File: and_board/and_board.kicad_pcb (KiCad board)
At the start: 2 copper layers, 39.7 x 31.6 mm, 12 parts, among them J1 SJ1-2503A, J2 SJ1-2503A, J3 SJ1-2503A, U1 SN74LS08N

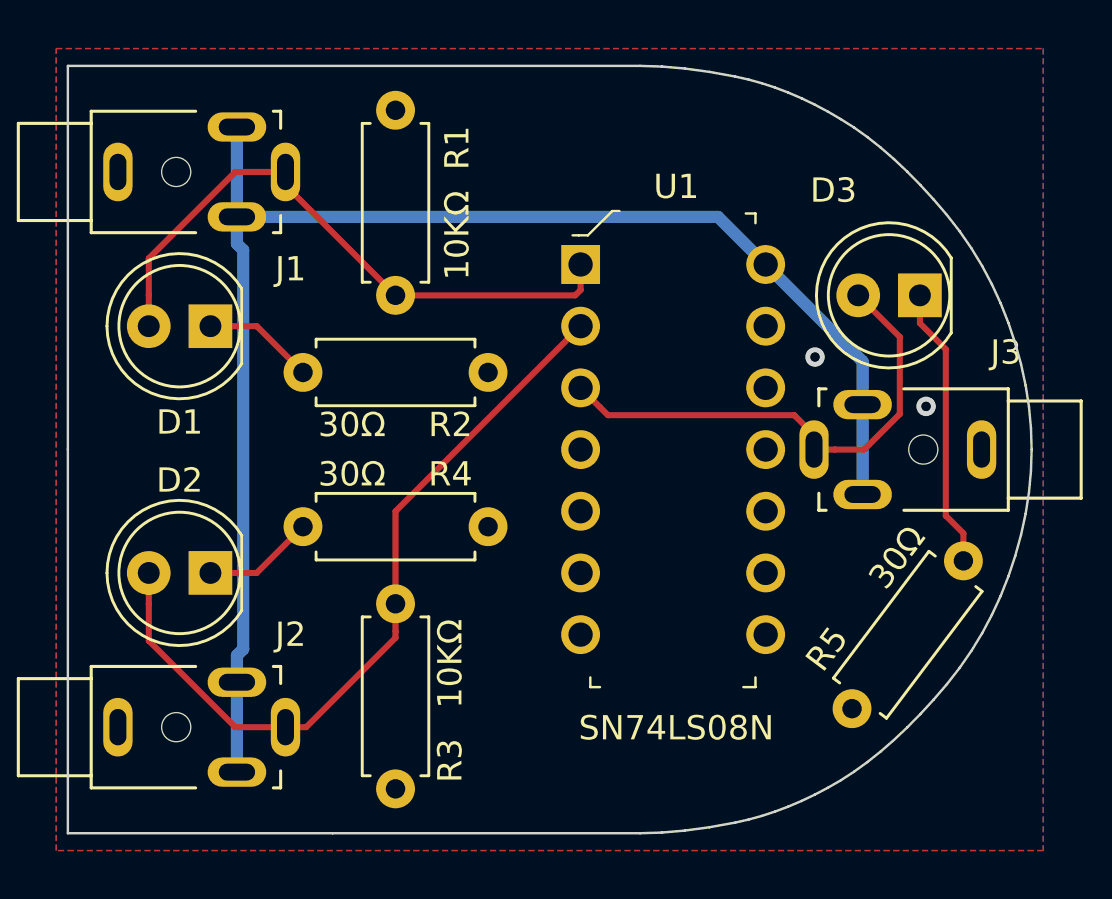
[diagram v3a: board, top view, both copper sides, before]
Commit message: Added truth table silk to and/or boards
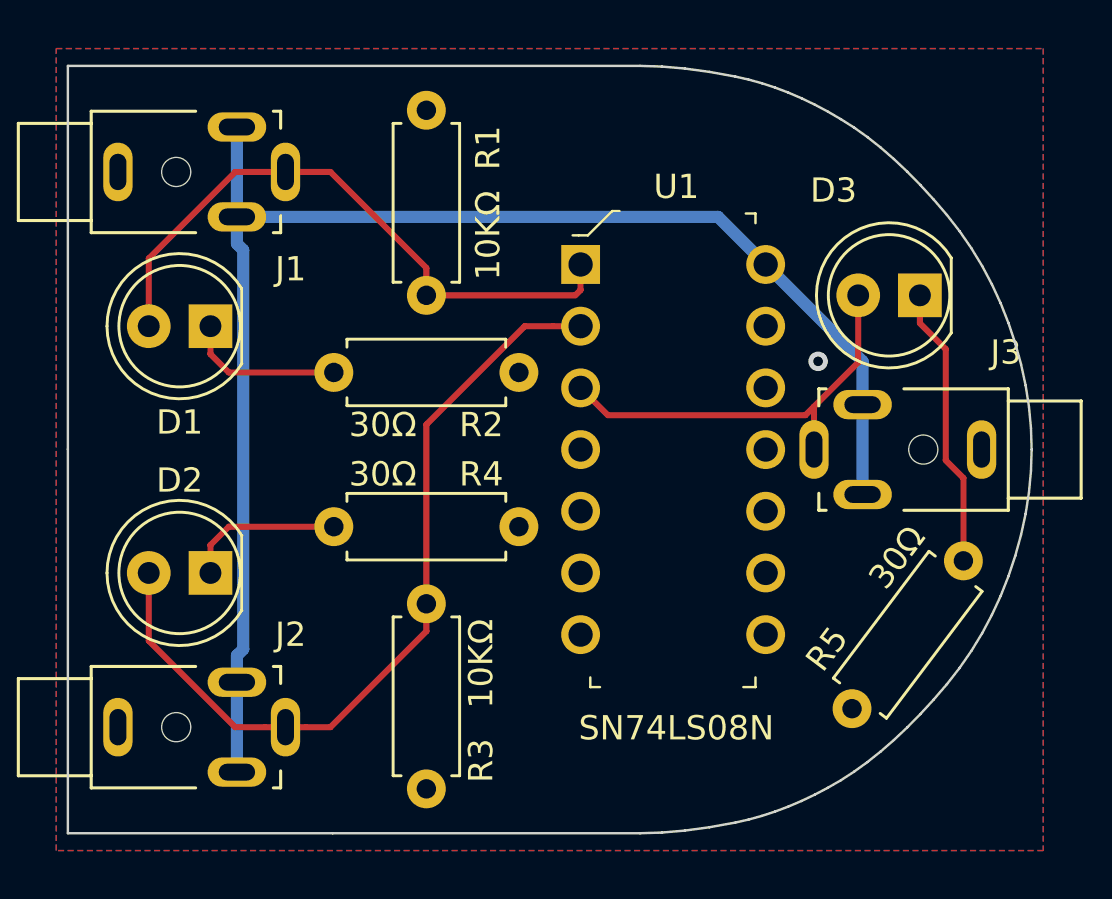
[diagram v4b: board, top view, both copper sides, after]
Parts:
- added Ref**: Val**, conduWIT_parts:and_truth_table, B.Cu at (149.4, 75.0)
- moved R1 1.27 mm to (144.8, 61.0)
- moved R2 1.27 mm to (148.6, 71.8)
- moved R3 1.27 mm to (144.8, 88.9)
- moved R4 1.27 mm to (148.6, 78.1)
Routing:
- net Net-(D3-Pad2): track 20.8 -> 17.3 mm
- net Net-(D2-Pad1): track 4.60 -> 6.54 mm
- net Net-(D1-Pad1): track 4.60 -> 6.54 mm
- net Net-(D2-Pad2): track 31.9 -> 33.9 mm
- net GND: vias 2 -> 1

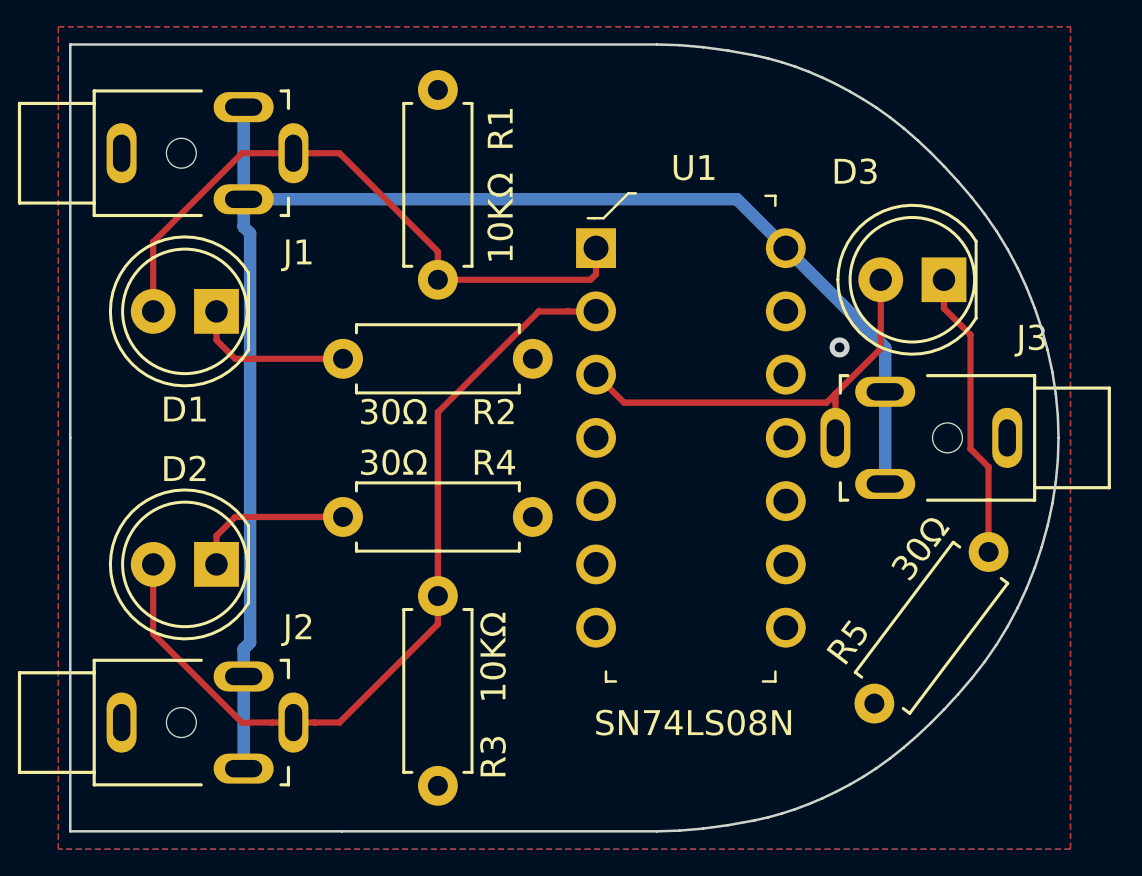
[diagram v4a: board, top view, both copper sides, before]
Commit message: Increased track width and clearance
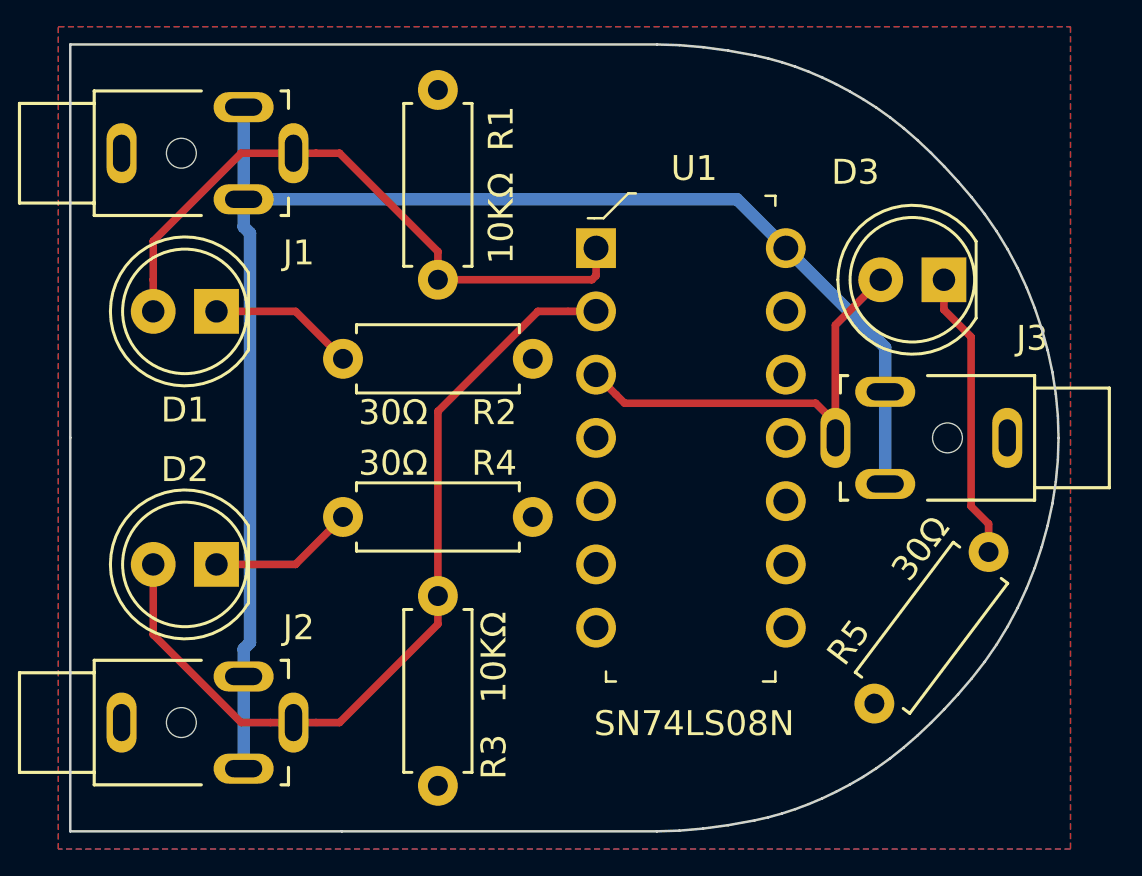
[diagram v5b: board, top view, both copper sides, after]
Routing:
- net Net-(D3-Pad2): track 17.3 -> 18.1 mm
- net Net-(D2-Pad1): track 6.54 -> 5.87 mm
- net Net-(D1-Pad1): track 6.54 -> 5.87 mm
- net GND: vias 1 -> 0
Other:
- net class Default: clearance 0.2 -> 0.19558; trace_width 0.25 -> 0.3048; via_dia 0.8 -> 0.5842; via_drill 0.4 -> 0.3302
- rule pad_to_mask_clearance: 0.051 -> 0
- rule trace_clearance: 0.2 -> 0.19558
- rule trace_min: 0.2 -> 0.3048
- rule via_min_drill: 0.3 -> 0.3302
- rule via_min_size: 0.4 -> 0.5842

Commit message: Final silkscreen touch-up
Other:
- board text added: "and_board 1.0.0 03/2020"
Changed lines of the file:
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@@
   (general
     (thickness 1.6)
-    (drawings 70)
+    (drawings 71)
     (tracks 51)
     (zones 0)
@@
     (0 F.Cu signal)
     (31 B.Cu signal)
-    (32 B.Adhes user hide)
-    (33 F.Adhes user hide)
-    (34 B.Paste user hide)
+    (32 B.Adhes user)
+    (33 F.Adhes user)
+    (34 B.Paste user)
     (35 F.Paste user)
-    (36 B.SilkS user hide)
+    (36 B.SilkS user)
     (37 F.SilkS user)
-    (38 B.Mask user hide)
+    (38 B.Mask user)
     (39 F.Mask user)
-    (40 Dwgs.User user hide)
-    (41 Cmts.User user hide)
-    (42 Eco1.User user hide)
-    (43 Eco2.User user hide)
+    (40 Dwgs.User user)
+    (41 Cmts.User user)
+    (42 Eco1.User user)
+    (43 Eco2.User user)
     (44 Edge.Cuts user)
-    (45 Margin user hide)
-    (46 B.CrtYd user hide)
-    (47 F.CrtYd user hide)
-    (48 B.Fab user hide)
-    (49 F.Fab user hide)
+    (45 Margin user)
+    (46 B.CrtYd user)
+    (47 F.CrtYd user)
+    (48 B.Fab user)
+    (49 F.Fab user)
   )
   (setup
@@
     (visible_elements 7FFFFFFF)
     (pcbplotparams
-      (layerselection 0x010fc_ffffffff)
-      (usegerberextensions false)
+      (layerselection 0x010f0_ffffffff)
+      (usegerberextensions true)
       (usegerberattributes false)
       (usegerberadvancedattributes false)
@@
       (outputformat 1)
       (mirror false)
-      (drillshape 1)
+      (drillshape 0)
       (scaleselection 1)
-      (outputdirectory ""))
+      (outputdirectory "mfg"))
   )
   (net 0 "")
@@
     )
   )
+  (gr_text "and_board\n1.0.0\n03/2020" (at 133.985 74.93 90) (layer B.SilkS)
+    (effects (font (size 1 1) (thickness 0.15)) (justify mirror))
+  )
   (gr_line (start 130.019472 59.132977) (end 153.574584 59.132977) (layer Edge.Cuts) (width 0.1))

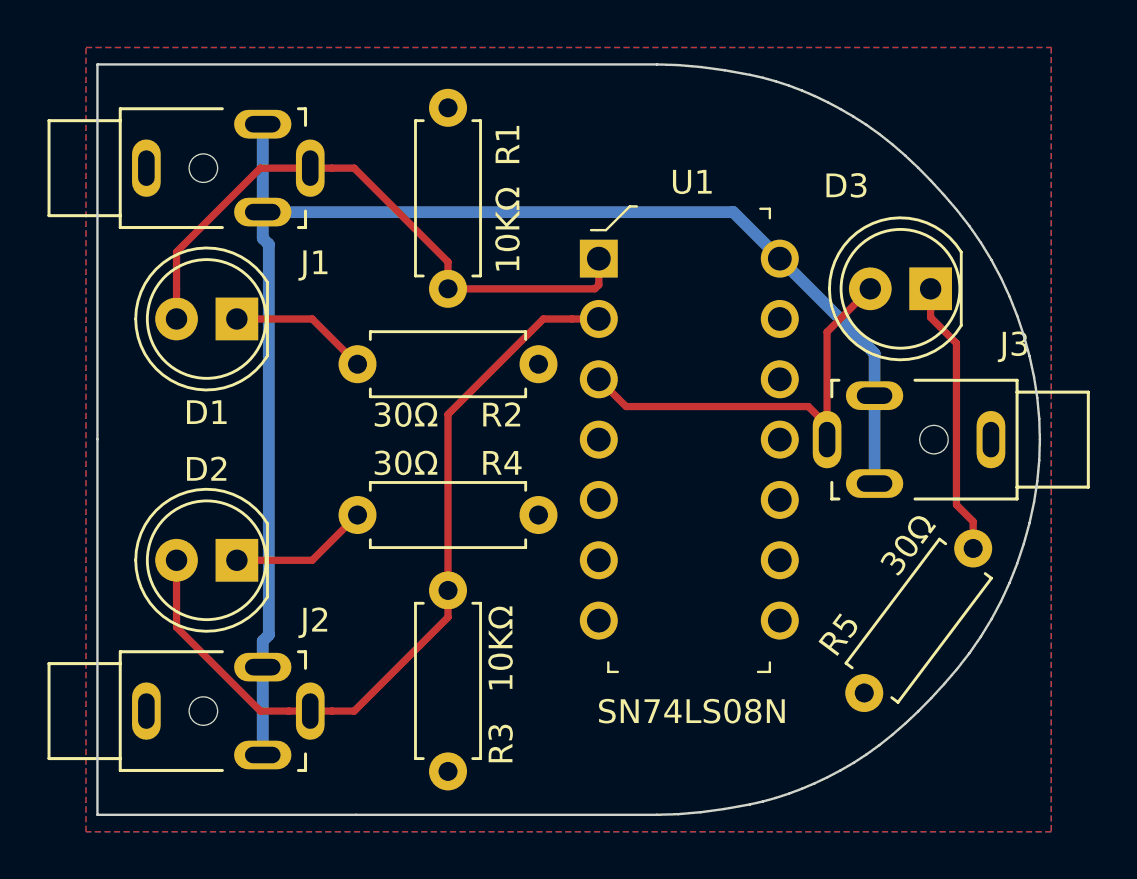
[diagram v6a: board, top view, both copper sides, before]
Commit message: Update resistor values, clean schematic
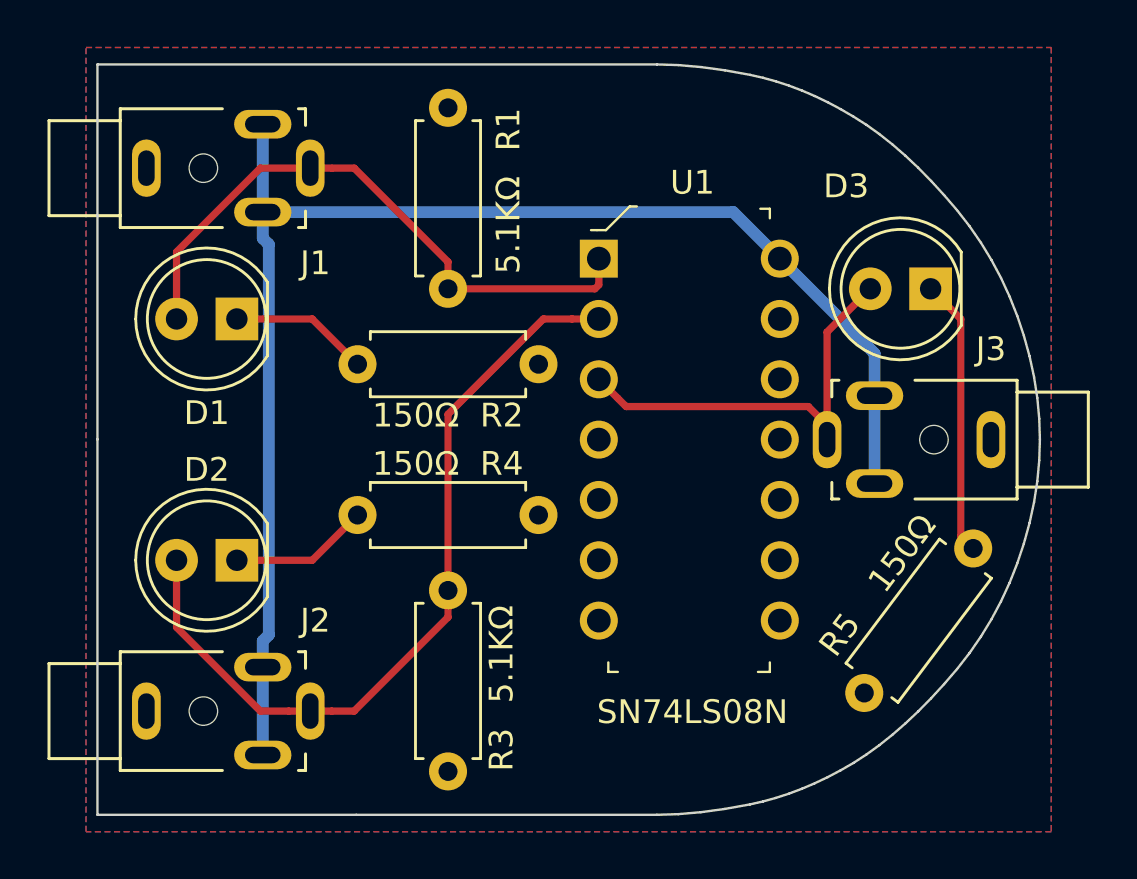
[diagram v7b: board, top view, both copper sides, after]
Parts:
- removed Ref**: Val**, conduWIT_parts:and_truth_table
- R1, R3: value 10KΩ -> 5.1KΩ
- R2, R4, R5: value 30Ω -> 150Ω
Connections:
- U1 pad 10: (no net) -> unconnected-(U1-Pad10)
- U1 pad 11: (no net) -> unconnected-(U1-Pad11)
- U1 pad 12: (no net) -> unconnected-(U1-Pad12)
- U1 pad 13: (no net) -> unconnected-(U1-Pad13)
- U1 pad 4: (no net) -> unconnected-(U1-Pad4)
- U1 pad 5: (no net) -> unconnected-(U1-Pad5)
- U1 pad 6: (no net) -> unconnected-(U1-Pad6)
- U1 pad 8: (no net) -> unconnected-(U1-Pad8)
- U1 pad 9: (no net) -> unconnected-(U1-Pad9)
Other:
- net class Default removed
- board text added: "and_board 1.0.1 01/2023"
- board text removed: "and_board 1.0.0 03/2020"

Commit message: Readd truth table
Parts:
- added Ref**: Val**, conduWIT_parts:and_truth_table, B.Cu at (149.5, 74.9)
